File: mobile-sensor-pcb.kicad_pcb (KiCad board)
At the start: 2 copper layers, 101.6 x 53.3 mm, 83 parts, among them J1 SMA, J2 USB_OTG, J3 JST PH, Q1 PNP-BJT-BIASED_SOT, SW1 RESET, SW2 OS102011MA1QS1, U1 3M_2908-05WB-MG, U10 LP2980AIM5-3.3/NOPB, U11 LP2980AIM5-3.3/NOPB, U12 LP2980AIM5-3.3/NOPB, U13 TPS61030RSA, U2 74HC4050, U3 FGPMMOPA6H, U4 RT9193, U5 MIC5219, U6 MCP73831T-2ACI/OT, U7 MAX31855KASA, U8 MAX31855KASA, U9 MAX31855KASA, X1 XBEE

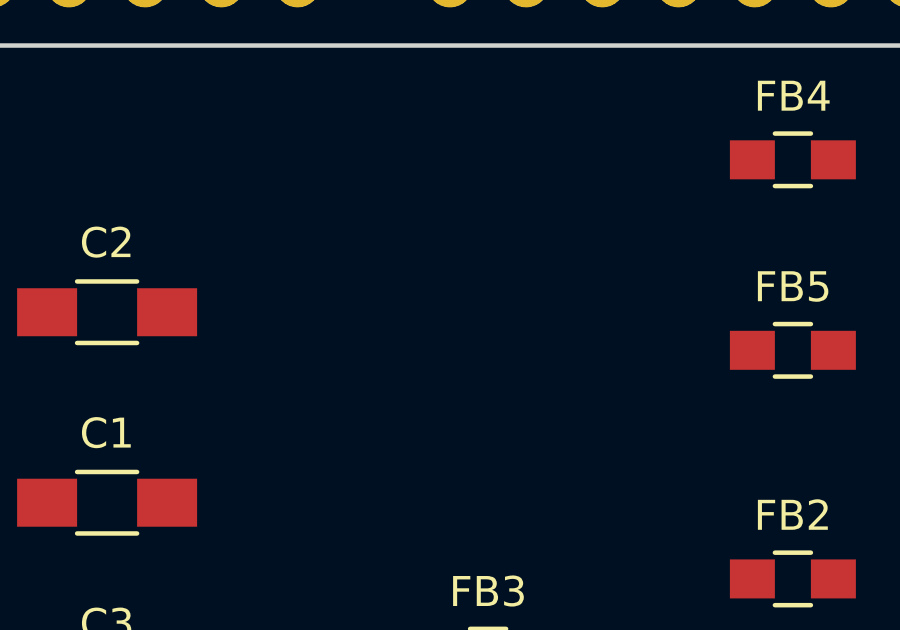
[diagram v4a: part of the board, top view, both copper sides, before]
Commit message: Start connecting stuff. Still need a few more resistors.
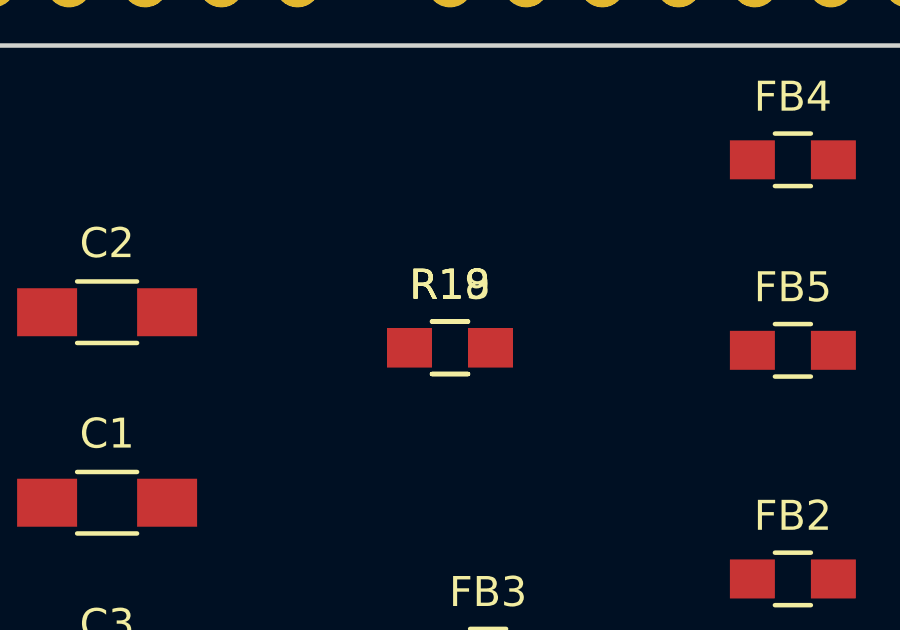
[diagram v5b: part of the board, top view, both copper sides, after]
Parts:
- added R18, R19: 10k, Resistors_SMD:R_0805_HandSoldering, F.Cu at (101.6, 162.5)
- LED1: value RED: XBEE DOUT -> RX
- LED10: value YELLOW: SD CARD DATA -> LOG
- LED11: value GREEN: GPS 3.3 V -> PWR
- LED12: value RED: GPS FIX -> FIX
- LED2: value GREEN: XBEE DIN -> TX
- LED3: value GREEN: XBEE SIGNAL STRENGTH -> SIG
- LED4: value RED: XBEE 3.3 V -> PWR
- LED5: value GREEN: XBEE CONNECTED -> CONN
- LED6: value BLUE: 5 V -> 5V
- LED7: value GREEN: BATTERY FULL -> FULL
- LED8: value YELLOW: BATTERY CHARGING -> CHG
- LED9: value RED: BATTERY DYING -> DEAD
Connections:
- net Net-(LED10-Pad2) renamed SD-CLK
- net Net-(LED8-Pad2) renamed USB-5V
- net Net-(U2-Pad3) renamed DUE-SCK
- net Net-(U2-Pad5) renamed DUE-MOSI
- BT1 pad 2: Net-(BT1-Pad2) -> GND
- C1 pad 2: Net-(C1-Pad2) -> GND
- C10 pad 1: Net-(C10-Pad1) -> GPS-SD-3V3
- C10 pad 2: Net-(C10-Pad2) -> GND
- C13 pad 2: Net-(C13-Pad2) -> GND
- C14 pad 2: Net-(C14-Pad2) -> GND
- C15 pad 1: Net-(C15-Pad1) -> RESET
- C16 pad 2: Net-(C16-Pad2) -> GND
- C2 pad 2: Net-(C2-Pad2) -> GND
- C20 pad 1: Net-(C20-Pad1) -> Net-(C13-Pad1)
- C20 pad 2: Net-(C20-Pad2) -> GND
- C9 pad 1: Net-(C9-Pad1) -> BATT-5V
- C9 pad 2: Net-(C9-Pad2) -> GND
- D1 pad 1: Net-(D1-Pad1) -> BATT-5V
- F1 pad 1: Net-(F1-Pad1) -> Net-(D1-Pad2)
- F1 pad 2: Net-(F1-Pad2) -> Net-(C13-Pad1)
- FB7 pad 1: Net-(FB7-Pad1) -> GPS-SD-3V3
- J1 pad 2: Net-(J1-Pad2) -> GND
- J1 pad 5: Net-(J1-Pad5) -> GND
- LED1 pad 2: Net-(LED1-Pad2) -> XBEE-3V3
- LED11 pad 2: Net-(LED11-Pad2) -> GPS-SD-3V3
- LED12 pad 2: Net-(LED12-Pad2) -> GPS-FIX
- LED2 pad 2: Net-(LED2-Pad2) -> XBEE-3V3
- LED3 pad 2: Net-(LED3-Pad2) -> XBEE-RSSI
- LED4 pad 2: Net-(LED4-Pad2) -> XBEE-3V3
- LED5 pad 2: Net-(LED5-Pad2) -> XBEE-DIO5
- LED6 pad 2: Net-(LED6-Pad2) -> BATT-5V
- LED7 pad 2: Net-(LED7-Pad2) -> BATT-STAT
- LED9 pad 2: Net-(LED9-Pad2) -> BATT-DEAD
- Q1 pad 2: Net-(Q1-Pad2) -> BATT-5V
- Q1 pad 3: Net-(Q1-Pad3) -> BATT-DEAD
- R1 pad 2: Net-(R1-Pad2) -> XBEE-DOUT
- R2 pad 2: Net-(R2-Pad2) -> XBEE-DIN
- R8 pad 2: Net-(R8-Pad2) -> BATT-STAT
- SHIELD1 pad 0: Net-(SHIELD1-Pad0) -> DUE-5V-RX
- SHIELD1 pad 1: Net-(SHIELD1-Pad1) -> DUE-TX
- U1 pad 4: Net-(U1-Pad4) -> GPS-SD-3V3
- U1 pad 6: Net-(U1-Pad6) -> GND
- U1 pad 9: Net-(U1-Pad9) -> GND
- U13 pad 1: Net-(U13-Pad1) -> Net-(C13-Pad1)
- U13 pad 16: Net-(U13-Pad16) -> Net-(C13-Pad1)
- U13 pad 17: Net-(U13-Pad17) -> GND
- U13 pad 5: Net-(U13-Pad5) -> GND
- U2 pad 1: Net-(U2-Pad1) -> GPS-SD-3V3
- U2 pad 11: Net-(U2-Pad11) -> DUE-5V-RX
- U2 pad 12: Net-(U2-Pad12) -> GPS-3V3-RX
- U2 pad 2: Net-(U2-Pad2) -> Net-(U1-Pad5)
- U2 pad 4: Net-(U2-Pad4) -> Net-(U1-Pad3)
- U2 pad 6: Net-(U2-Pad6) -> Net-(U1-Pad2)
- U2 pad 8: Net-(U2-Pad8) -> GND
- U3 pad 1: Net-(U3-Pad1) -> Net-(FB7-Pad2)
- U3 pad 10: Net-(U3-Pad10) -> GPS-3V3-RX
- U3 pad 11: Net-(U3-Pad11) -> Net-(J1-Pad1)
- U3 pad 19: Net-(U3-Pad19) -> GND
- U3 pad 3: Net-(U3-Pad3) -> GND
- U3 pad 4: Net-(U3-Pad4) -> Net-(BT1-Pad1)
- U3 pad 5: Net-(U3-Pad5) -> GPS-FIX
- U3 pad 9: Net-(U3-Pad9) -> DUE-TX
- U4 pad 1: Net-(U4-Pad1) -> BATT-5V
- U4 pad 2: Net-(U4-Pad2) -> GND
- U4 pad 3: Net-(U4-Pad3) -> BATT-5V
- U4 pad 5: Net-(U4-Pad5) -> GPS-SD-3V3
- U5 pad 1: Net-(U5-Pad1) -> BATT-5V
- U5 pad 2: Net-(U5-Pad2) -> GND
- U5 pad 3: Net-(U5-Pad3) -> BATT-5V
- U5 pad 5: Net-(U5-Pad5) -> XBEE-3V3
- X1 pad 1: Net-(X1-Pad1) -> XBEE-3V3
- X1 pad 10: Net-(X1-Pad10) -> GND
- X1 pad 15: Net-(X1-Pad15) -> XBEE-DIO5
- X1 pad 17: Net-(X1-Pad17) -> Net-(C15-Pad2)
- X1 pad 2: Net-(X1-Pad2) -> XBEE-DOUT
- X1 pad 3: Net-(X1-Pad3) -> XBEE-DIN
- X1 pad 4: Net-(X1-Pad4) -> RESET
- X1 pad 6: Net-(X1-Pad6) -> XBEE-RSSI

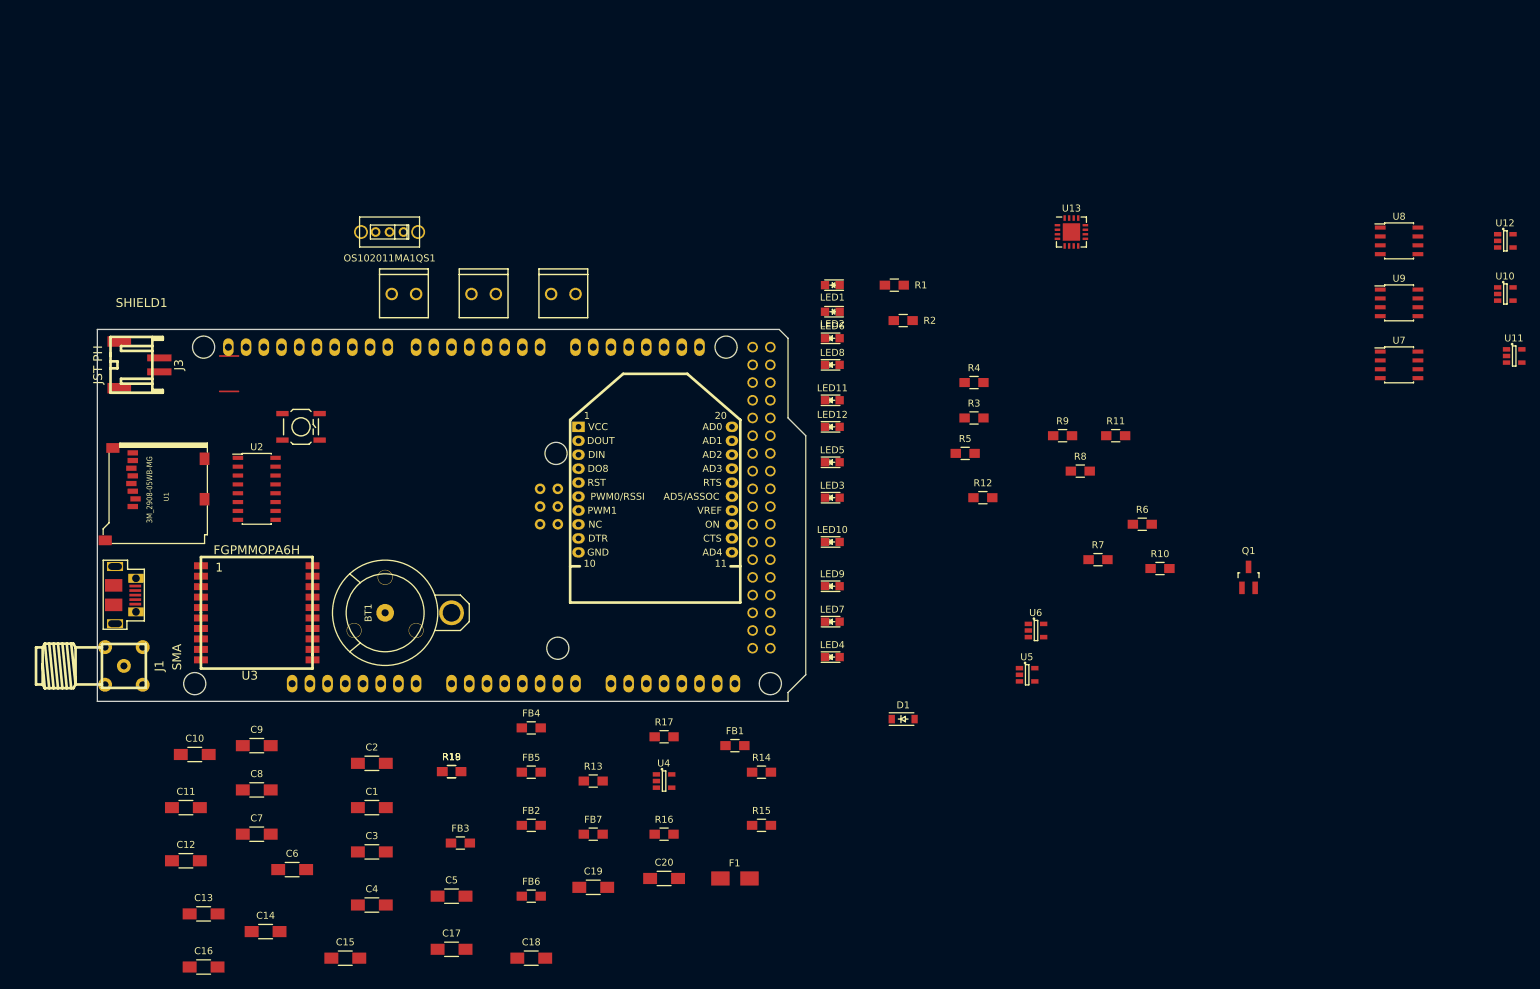
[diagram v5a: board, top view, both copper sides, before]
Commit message: Schematic done
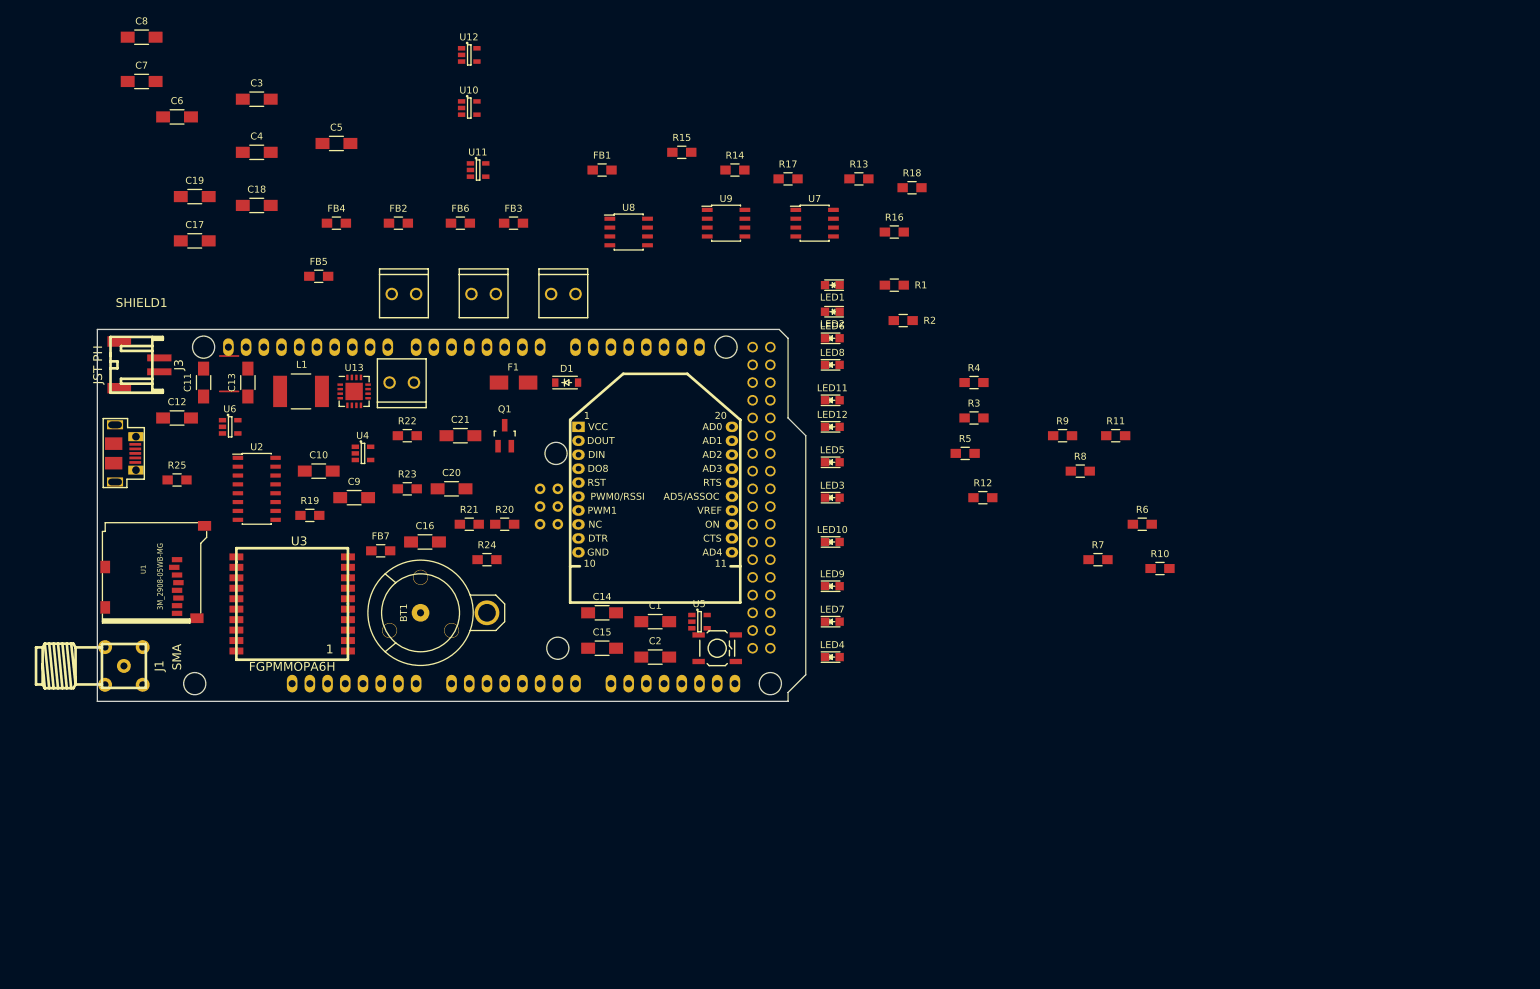
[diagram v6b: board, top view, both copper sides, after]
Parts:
- added C21: 2.2 uF, Capacitors_SMD:C_1206_HandSoldering, F.Cu at (102.9, 114.3)
- added L1: 6.8uH, Inductors_NEOSID:Neosid_Inductor_SM-NE56_SMD2220, F.Cu at (80.0, 108.0)
- added R20: 340k, Resistors_SMD:R_0805_HandSoldering, F.Cu at (109.2, 127.0)
- added R21: 340k, Resistors_SMD:R_0805_HandSoldering, F.Cu at (104.1, 127.0)
- added R22: 200k, Resistors_SMD:R_0805_HandSoldering, F.Cu at (95.2, 114.3)
- added R23: 1.80M, Resistors_SMD:R_0805_HandSoldering, F.Cu at (95.2, 121.9)
- added R24: 1.80M, Resistors_SMD:R_0805_HandSoldering, F.Cu at (106.7, 132.1)
- added R25: 2k, Resistors_SMD:R_0805_HandSoldering, F.Cu at (62.2, 120.7)
- C13: value 2.2 uF -> 100nF
- SW2: value OS102011MA1QS1 -> ON/OFF; footprint rascalmicro_kicad_footprints:OS102011MA1QS1 -> freetronics_footprints:SCREWTERMINAL-3.5MM-2
- moved U11 151.0 mm to (105.4, 76.2)
- moved U10 151.0 mm to (104.1, 67.3)
- moved U12 151.0 mm to (104.1, 59.7)
- moved U6 119.2 mm to (69.8, 113.0)
- moved C18 114.9 mm to (73.7, 81.3)
- moved C19 114.4 mm to (64.8, 80.0)
- moved U8 110.5 mm to (127.0, 85.1)
- moved C4 109.2 mm to (73.7, 73.7)
- moved C3 109.2 mm to (73.7, 66.0)
- moved C5 109.2 mm to (85.1, 72.4)
- moved C6 109.2 mm to (62.2, 68.6)
- moved C7 109.2 mm to (57.1, 63.5)
- moved C8 109.2 mm to (57.1, 57.1)
- moved Q1 108.6 mm to (109.2, 114.3)
- moved C17 108.1 mm to (64.8, 86.4)
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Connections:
- C11 pad 2: Net-(C11-Pad2) -> GND
- C12 pad 1: Net-(C12-Pad1) -> USB-5V
- C12 pad 2: Net-(C12-Pad2) -> GND
- C13 pad 1: Net-(C13-Pad1) -> Net-(C11-Pad1)
- C15 pad 1: RESET -> XBEE-RESET
- C20 pad 1: Net-(C13-Pad1) -> Net-(C20-Pad1)
- C3 pad 2: Net-(C3-Pad2) -> GND
- C4 pad 1: Net-(C4-Pad1) -> Net-(C3-Pad1)
- C4 pad 2: Net-(C4-Pad2) -> GND
- C5 pad 2: Net-(C5-Pad2) -> GND
- C6 pad 1: Net-(C6-Pad1) -> Net-(C5-Pad1)
- C6 pad 2: Net-(C6-Pad2) -> GND
- C7 pad 2: Net-(C7-Pad2) -> GND
- C8 pad 1: Net-(C8-Pad1) -> Net-(C7-Pad1)
- C8 pad 2: Net-(C8-Pad2) -> GND
- F1 pad 2: Net-(C13-Pad1) -> Net-(C20-Pad1)
- FB1 pad 2: Net-(FB1-Pad2) -> Net-(C17-Pad1)
- FB2 pad 2: Net-(FB2-Pad2) -> Net-(C17-Pad2)
- FB3 pad 2: Net-(FB3-Pad2) -> Net-(C18-Pad1)
- FB4 pad 2: Net-(FB4-Pad2) -> Net-(C18-Pad2)
- FB5 pad 2: Net-(FB5-Pad2) -> Net-(C19-Pad1)
- FB6 pad 2: Net-(FB6-Pad2) -> Net-(C19-Pad2)
- J2 pad 1: Net-(J2-Pad1) -> USB-5V
- J2 pad 5: Net-(J2-Pad5) -> GND
- J3 pad 1: Net-(J3-Pad1) -> Net-(C11-Pad1)
- J3 pad 2: Net-(J3-Pad2) -> GND
- R1 pad 2: XBEE-DOUT -> XBEE-RX
- R13 pad 2: Net-(R13-Pad2) -> TC-SCK
- R14 pad 1: Net-(R14-Pad1) -> Net-(C3-Pad1)
- R14 pad 2: Net-(R14-Pad2) -> TC-CS0
- R15 pad 2: Net-(R15-Pad2) -> TC-SCK
- R16 pad 1: Net-(R16-Pad1) -> Net-(C5-Pad1)
- R16 pad 2: Net-(R16-Pad2) -> TC-CS1
- R17 pad 2: Net-(R17-Pad2) -> TC-SCK
- R18 pad 1: Net-(R18-Pad1) -> Net-(C7-Pad1)
- R18 pad 2: Net-(R18-Pad2) -> TC-CS2
- R19 pad 2: Net-(R19-Pad2) -> SD-CS
- R2 pad 2: XBEE-DIN -> XBEE-TX
- SHIELD1 pad 0: DUE-5V-RX -> Net-(SHIELD1-Pad0)
- SHIELD1 pad 1: DUE-TX -> Net-(SHIELD1-Pad1)
- SHIELD1 pad 10: Net-(SHIELD1-Pad10) -> TC-CS0
- SHIELD1 pad 16: Net-(SHIELD1-Pad16) -> XBEE-TX
- SHIELD1 pad 17: Net-(SHIELD1-Pad17) -> XBEE-RX
- SHIELD1 pad 18: Net-(SHIELD1-Pad18) -> GPS-TX
- SHIELD1 pad 19: Net-(SHIELD1-Pad19) -> GPS-5V-RX
- SHIELD1 pad 4: Net-(SHIELD1-Pad4) -> TC-CS1
- SHIELD1 pad 44: Net-(SHIELD1-Pad44) -> SD-CS
- SHIELD1 pad 46: Net-(SHIELD1-Pad46) -> SD-MOSI
- SHIELD1 pad 48: Net-(SHIELD1-Pad48) -> SD-MISO
- SHIELD1 pad 50: Net-(SHIELD1-Pad50) -> SD-SCK
- SHIELD1 pad 52: Net-(SHIELD1-Pad52) -> TC-CS2
- SHIELD1 pad 5V: Net-(SHIELD1-Pad5V) -> BATT-5V
- SHIELD1 pad 5V_4: Net-(SHIELD1-Pad5V_4) -> BATT-5V
- SHIELD1 pad 5V_5: Net-(SHIELD1-Pad5V_5) -> BATT-5V
- SHIELD1 pad GND1: Net-(SHIELD1-PadGND1) -> GND
- SHIELD1 pad GND2: Net-(SHIELD1-PadGND2) -> GND
- SHIELD1 pad GND3: Net-(SHIELD1-PadGND3) -> GND
- SHIELD1 pad GND4: Net-(SHIELD1-PadGND4) -> GND
- SHIELD1 pad GND5: Net-(SHIELD1-PadGND5) -> GND
- SHIELD1 pad RST: Net-(SHIELD1-PadRST) -> XBEE-RESET
- SHIELD1 pad SP1: Net-(SHIELD1-PadSP1) -> TC-MISO
- SHIELD1 pad SP3: Net-(SHIELD1-PadSP3) -> TC-SCK
- SHIELD1 pad SP6: Net-(SHIELD1-PadSP6) -> GND
- SW1 pad 1: Net-(SW1-Pad1) -> XBEE-RESET
- SW1 pad 2: Net-(SW1-Pad2) -> GND
- SW2 pad 1: Net-(SW2-Pad1) -> GND
- SW2 pad 2: Net-(SW2-Pad2) -> Net-(R21-Pad1)
- TC1 pad 1: Net-(TC1-Pad1) -> Net-(FB2-Pad1)
- TC1 pad 2: Net-(TC1-Pad2) -> Net-(FB1-Pad1)
- TC2 pad 1: Net-(TC2-Pad1) -> Net-(FB4-Pad1)
- TC2 pad 2: Net-(TC2-Pad2) -> Net-(FB3-Pad1)
- TC3 pad 1: Net-(TC3-Pad1) -> Net-(FB6-Pad1)
- TC3 pad 2: Net-(TC3-Pad2) -> Net-(FB5-Pad1)
- U1 pad 7: Net-(U1-Pad7) -> SD-MISO
- U10 pad 1: Net-(U10-Pad1) -> BATT-5V
- U10 pad 2: Net-(U10-Pad2) -> GND
- U10 pad 3: Net-(U10-Pad3) -> BATT-5V
- U10 pad 5: Net-(U10-Pad5) -> Net-(C3-Pad1)
- U11 pad 1: Net-(U11-Pad1) -> BATT-5V
- U11 pad 2: Net-(U11-Pad2) -> GND
- U11 pad 3: Net-(U11-Pad3) -> BATT-5V
- U11 pad 5: Net-(U11-Pad5) -> Net-(C5-Pad1)
- U12 pad 2: Net-(U12-Pad2) -> GND
- U12 pad 3: Net-(U12-Pad3) -> Net-(U12-Pad1)
- U12 pad 5: Net-(U12-Pad5) -> Net-(C7-Pad1)
- U13 pad 1: Net-(C13-Pad1) -> Net-(C20-Pad1)
- U13 pad 10: Net-(U13-Pad10) -> GND
- U13 pad 11: Net-(U13-Pad11) -> Net-(R21-Pad1)
- U13 pad 13: Net-(U13-Pad13) -> GND
- U13 pad 16: Net-(C13-Pad1) -> Net-(C20-Pad1)
- U13 pad 2: Net-(U13-Pad2) -> Net-(L1-Pad2)
- U13 pad 3: Net-(U13-Pad3) -> Net-(L1-Pad2)
- U13 pad 8: Net-(U13-Pad8) -> Net-(C11-Pad1)
- U2 pad 11: DUE-5V-RX -> GPS-5V-RX
- U2 pad 3: DUE-SCK -> SD-SCK
- U2 pad 5: DUE-MOSI -> SD-MOSI
- U2 pad 7: Net-(R19-Pad2) -> SD-CS
- U3 pad 9: DUE-TX -> GPS-TX
- U6 pad 1: Net-(U6-Pad1) -> BATT-STAT
- U6 pad 2: Net-(U6-Pad2) -> GND
- U6 pad 3: Net-(U6-Pad3) -> Net-(C11-Pad1)
- U6 pad 4: Net-(U6-Pad4) -> USB-5V
- U7 pad 1: Net-(U7-Pad1) -> GND
- U7 pad 2: Net-(U7-Pad2) -> Net-(C17-Pad2)
- U7 pad 3: Net-(U7-Pad3) -> Net-(C17-Pad1)
- U7 pad 4: Net-(U7-Pad4) -> Net-(C3-Pad1)
- U7 pad 5: Net-(U7-Pad5) -> TC-SCK
- U7 pad 6: Net-(U7-Pad6) -> TC-CS0
- U7 pad 7: Net-(U7-Pad7) -> TC-MISO
- U8 pad 1: Net-(U8-Pad1) -> GND
- U8 pad 2: Net-(U8-Pad2) -> Net-(C18-Pad2)
- U8 pad 3: Net-(U8-Pad3) -> Net-(C18-Pad1)
- U8 pad 4: Net-(U8-Pad4) -> Net-(C5-Pad1)
- U8 pad 5: Net-(U8-Pad5) -> TC-SCK
- U8 pad 6: Net-(U8-Pad6) -> TC-CS1
- U8 pad 7: Net-(U8-Pad7) -> TC-MISO
- U9 pad 1: Net-(U9-Pad1) -> GND
- U9 pad 2: Net-(U9-Pad2) -> Net-(C19-Pad2)
- U9 pad 3: Net-(U9-Pad3) -> Net-(C19-Pad1)
- U9 pad 4: Net-(U9-Pad4) -> Net-(C7-Pad1)
- U9 pad 5: Net-(U9-Pad5) -> TC-SCK
- U9 pad 6: Net-(U9-Pad6) -> TC-CS2
- U9 pad 7: Net-(U9-Pad7) -> TC-MISO
- X1 pad 2: XBEE-DOUT -> XBEE-RX
- X1 pad 3: XBEE-DIN -> XBEE-TX
- X1 pad 4: RESET -> Net-(X1-Pad4)
